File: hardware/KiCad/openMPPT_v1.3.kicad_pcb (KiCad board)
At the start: 2 copper layers, 70 x 80 mm, 135 parts, among them Q1 BSC030N08NS5, Q2 BSC030N08NS5, Q3 BSC030N08NS5, Q4 BSC030N08NS5, U1 STM32F072RBT6, U2 CC6937S8-3FB020, U3 CC6937S8-3FB020, U4 SCT2A25STER, U5 SY8120B1ABC

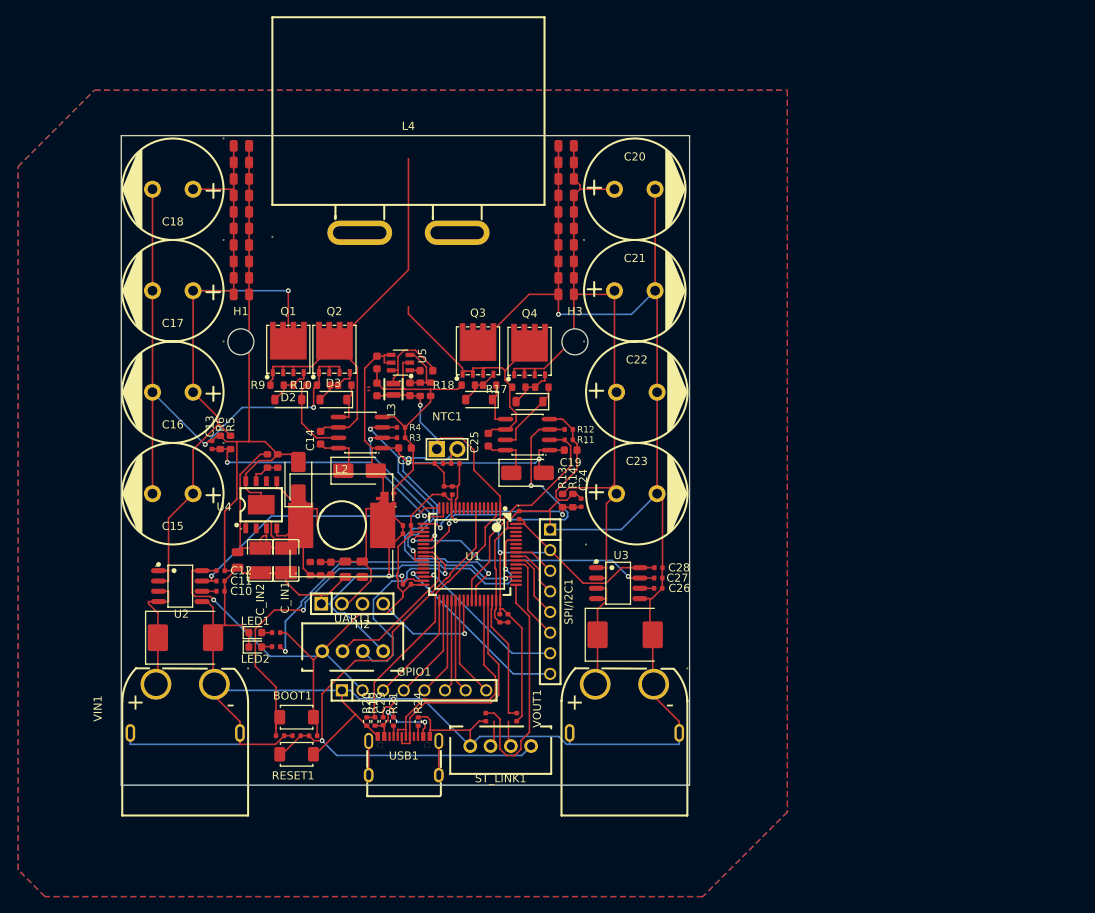
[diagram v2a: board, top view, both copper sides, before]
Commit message: hardware: import prior PCB layout work into current project
The current openMPPT_v1.3.kicad_pcb had footprints placed but zero
routing - the project's own PCB layout hadn't been started yet under
this repo structure. Real placement work already existed on the
now-stale feature/pcb-v1.3 branch (commit fe1c635 "started layout"),
done before the hardware/ reorg to the current file naming and library
layout. That branch never got merged and diverged too far from main to
merge normally, but the PCB layout itself is real prior work, not
throwaway - importing it here as the starting point instead of
re-placing 135 footprints from scratch.

Same KiCad file format version (20260206, pcbnew 10.0) on both sides,
so no format migration needed. Footprint/net sync against the current
schematic (which has moved on since this layout was done - D9 removed,
inductor/TVS parts changed) is the user's job in KiCad (Update PCB from
Schematic), not attempted here.

Co-Authored-By: Claude Sonnet 5 <noreply@anthropic.com>
Claude-Session: https://claude.ai/code/session_018pci5pMUxpfFa5RN5eKA6b
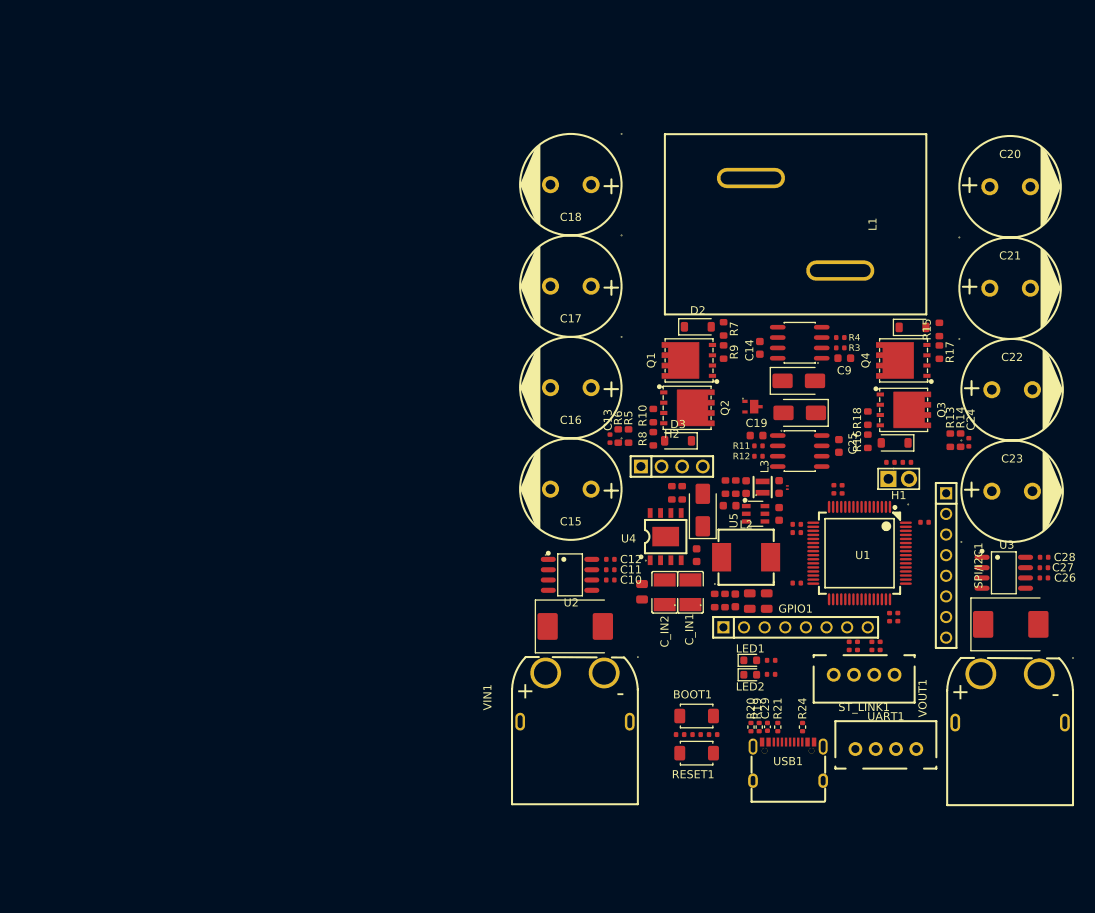
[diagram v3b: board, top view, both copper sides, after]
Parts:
- removed C1, C2, C3, C37, C38, C39, C4, C40, C41, C42, C43, C44, C45, C46, C47, C48, C5, C6, C7, C8: 100nF, PCM_JLCPCB:C_0805
- removed H3: MountingHole, MountingHole:MountingHole_3.2mm_M3_DIN965
- removed L4: HCZH-3218-150-M, easyeda2kicad:IND-TH_L33.5-W23.0-P12.00_HCZH-3218
- removed NTC1: TEMP, easyeda2kicad:HDR-TH_2P-P2.54-V-M
- removed R36, R37, R38, R39: 2.2Ω, PCM_JLCPCB:R_0603
- added L1: 47uH, easyeda2kicad:IND-TH_L32.2-W22.2_CPEX3222L, F.Cu at (133.9, 61.7)
- added R15: 5.1Ω, PCM_JLCPCB:R_0603, F.Cu at (151.6, 74.7)
- added R16: 5.1Ω, PCM_JLCPCB:R_0603, F.Cu at (142.8, 88.5)
- added R27: 47Ω, PCM_JLCPCB:R_0402, F.Cu at (143.3, 113.7)
- added R28: 47Ω, PCM_JLCPCB:R_0402, F.Cu at (141.5, 113.7)
- added R7: 5.1Ω, PCM_JLCPCB:R_0603, F.Cu at (125.0, 74.6)
- added R8: 5.1Ω, PCM_JLCPCB:R_0603, F.Cu at (116.3, 88.1)
- C14, C25: value 1uF -> 470nF
- D1, D4: value SS210 -> US1M
- D2, D3, D5, D6: value SS210 -> 1N4148W
- H1: value MountingHole -> TEMP; footprint MountingHole:MountingHole_3.2mm_M3_DIN965 -> easyeda2kicad:HDR-TH_2P-P2.54-V-M
- L2: footprint easyeda2kicad:IND-SMD_L12.5-W12.5-1 -> easyeda2kicad:IND-SMD_L7.7-W6.6_APS07A30M220
- LED1: value KT-0603R -> 19-213/Y2C-CQ2R2L/3T(CY)
- moved H1 82.8 mm to (146.6, 93.1)
- moved UART1 66.8 mm to (145.0, 126.3)
- moved LED1 61.1 mm to (128.3, 115.4)
- moved LED2 61.1 mm to (128.3, 117.2)
- moved R1 61.1 mm to (130.8, 115.4)
- moved R2 61.1 mm to (130.8, 117.2)
- moved R29 57.6 mm to (147.6, 91.0), turned to 0 degrees
- moved UA1 55.2 mm to (134.4, 76.3)
- moved C14 55.2 mm to (129.5, 76.9)
- moved C9 55.2 mm to (139.9, 78.2)
- moved D1 55.2 mm to (134.2, 81.0)
- moved R3 55.2 mm to (139.4, 76.9)
- moved R4 55.2 mm to (139.4, 75.7)
- moved R9 55.1 mm to (125.0, 77.5), turned to -90 degrees
- moved C31 53.6 mm to (145.5, 91.0), turned to 180 degrees
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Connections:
- net IN_CAP renamed Net-(C15-+)
- net OUT_CAP renamed Net-(C20-+)
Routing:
- net GND: track 582.1 -> 0.00 mm, vias 6 -> 0
- net 3V3: track 176.5 -> 0.00 mm, vias 5 -> 0
- net Net-(C20-+): track 90.9 -> 0.00 mm
- net Net-(C15-+): track 90.7 -> 0.00 mm, vias 1 -> 0
- net +10V: track 72.8 -> 0.00 mm, vias 2 -> 0
- net NRST: track 72.2 -> 0.00 mm, vias 1 -> 0
- net BOOT0: track 58.4 -> 0.00 mm, vias 2 -> 0
- net VS_A: track 54.8 -> 0.00 mm
- net TIM1_CH1N: track 37.6 -> 0.00 mm, vias 2 -> 0
- net LED: track 37.2 -> 0.00 mm, vias 2 -> 0
- net TIM1_CH2: track 37.2 -> 0.00 mm, vias 2 -> 0
- net VSENSEIN: track 34.5 -> 0.00 mm, vias 2 -> 0
- net ISENSEIN: track 34.0 -> 0.00 mm, vias 2 -> 0
- net VS_B: track 33.5 -> 0.00 mm
- net ISENSEOUT: track 33.2 -> 0.00 mm, vias 2 -> 0
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- removed copper zone on B.Cu, net GND
- removed copper zone on F.Cu, net GND
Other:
- board outline removed

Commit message: hardware: fix L4 footprint's broken 3D model path, sync PCB from schematic
The L4 footprint (IND-TH_L33.5-W23.0-P12.00_HCZH-3218) had a malformed
3D model path with a doubled directory segment:
${KIPRJMOD}/hardware/KiCad/libraries/... instead of
${KIPRJMOD}/libraries/... (KIPRJMOD already resolves to hardware/KiCad/,
the .kicad_pro's own directory) - so it silently failed to resolve,
looking like a missing/misaligned 3D model in the viewer rather than an
outright broken path. Re-saving the footprint in the Footprint Editor
fixed the path and, as a side effect, upgraded the whole file from the
legacy (module ...) format to the current (footprint "...") format -
KiCad does this automatically for any old-format footprint touched in a
new KiCad version.

Also includes the accumulated "Update PCB from Schematic" sync against
the current parts list (D9 removed, inductor swapped, etc. - the schema
has moved on since the imported layout was done on the old feature/pcb-v1.3
branch, per PR #8's description of remaining work).

Co-Authored-By: Claude Sonnet 5 <noreply@anthropic.com>
Claude-Session: https://claude.ai/code/session_018pci5pMUxpfFa5RN5eKA6b
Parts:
- removed D9: 3.3V, PCM_JLCPCB:D_DFN0603-2L
- removed L1: 47uH, easyeda2kicad:IND-TH_L32.2-W22.2_CPEX3222L
- removed R16: 5.1Ω, PCM_JLCPCB:R_0603
- removed R27, R28: 47Ω, PCM_JLCPCB:R_0402
- added C1: 100nF, PCM_JLCPCB:C_0805, F.Cu at (39.3, 84.5)
- added C2: 100nF, PCM_JLCPCB:C_0805, F.Cu at (39.3, 87.6)
- added C3: 100nF, PCM_JLCPCB:C_0805, F.Cu at (39.3, 90.6)
- added C37: 100nF, PCM_JLCPCB:C_0805, F.Cu at (43.8, 93.7)
- added C38: 100nF, PCM_JLCPCB:C_0805, F.Cu at (43.8, 96.7)
- added C39: 100nF, PCM_JLCPCB:C_0805, F.Cu at (48.2, 84.5)
- added C4: 100nF, PCM_JLCPCB:C_0805, F.Cu at (39.3, 93.7)
- added C40: 100nF, PCM_JLCPCB:C_0805, F.Cu at (48.2, 87.6)
- added C41: 100nF, PCM_JLCPCB:C_0805, F.Cu at (48.2, 90.6)
- added C42: 100nF, PCM_JLCPCB:C_0805, F.Cu at (48.2, 93.7)
- added C43: 100nF, PCM_JLCPCB:C_0805, F.Cu at (48.2, 96.7)
- added C44: 100nF, PCM_JLCPCB:C_0805, F.Cu at (52.7, 84.5)
- added C45: 100nF, PCM_JLCPCB:C_0805, F.Cu at (52.7, 87.6)
- added C46: 100nF, PCM_JLCPCB:C_0805, F.Cu at (52.7, 90.6)
- added C47: 100nF, PCM_JLCPCB:C_0805, F.Cu at (52.7, 93.7)
- added C48: 100nF, PCM_JLCPCB:C_0805, F.Cu at (52.7, 96.7)
- added C5: 100nF, PCM_JLCPCB:C_0805, F.Cu at (39.3, 96.7)
- added C6: 100nF, PCM_JLCPCB:C_0805, F.Cu at (43.8, 84.5)
- added C7: 100nF, PCM_JLCPCB:C_0805, F.Cu at (43.8, 87.6)
- added C8: 100nF, PCM_JLCPCB:C_0805, F.Cu at (43.8, 90.6)
- added H3: MountingHole, MountingHole:MountingHole_3.2mm_M3_DIN965, F.Cu at (91.0, 97.9)
- added L4: HCZH-3218-150-M, easyeda2kicad:IND-TH_L33.5-W23.0-P12.00_HCZH-3218, F.Cu at (133.6, 68.0)
- added NTC1: TEMP, easyeda2kicad:HDR-TH_2P-P2.54-V-M, F.Cu at (77.0, 55.7)
- added R36: 2.2Ω, PCM_JLCPCB:R_0603, F.Cu at (56.7, 84.1)
- added R37: 2.2Ω, PCM_JLCPCB:R_0603, F.Cu at (56.7, 86.4)
- added R38: 2.2Ω, PCM_JLCPCB:R_0603, F.Cu at (56.7, 88.6)
- added R39: 2.2Ω, PCM_JLCPCB:R_0603, F.Cu at (56.7, 90.9)
- C14, C25: value 470nF -> 1uF; footprint PCM_JLCPCB:C_0603 -> PCM_JLCPCB:C_0402
- D1, D4: value US1M -> SS210
- D2, D3, D5, D6: value 1N4148W -> SS210; footprint PCM_JLCPCB:D_SOD-123 -> PCM_JLCPCB:D_SMA
- H1: value TEMP -> MountingHole; footprint easyeda2kicad:HDR-TH_2P-P2.54-V-M -> MountingHole:MountingHole_3.2mm_M3_DIN965
- L2: footprint easyeda2kicad:IND-SMD_L7.7-W6.6_APS07A30M220 -> easyeda2kicad:IND-SMD_L12.5-W12.5-1
- LED1: value 19-213/Y2C-CQ2R2L/3T(CY) -> KT-0603R
- Q1, Q2, Q3, Q4: footprint easyeda2kicad:TDSON-8_L5.9-W5.2-P1.27-BL-1 -> easyeda2kicad:PG-TDSON-8_L5.0-W6.0-P1.27-BL-EP
- R15: value 5.1Ω -> 110kΩ
- R7, R8: value 5.1Ω -> 47Ω
- moved R30 1.56 mm to (123.9, 109.0)
- moved R35 1.56 mm to (118.6, 95.7)
- moved L2 1.56 mm to (126.5, 103.6)
- moved C32 1.56 mm to (125.2, 108.9)
- moved CC_Boot1 1.56 mm to (120.4, 103.4)
- moved C_IN1 1.56 mm to (119.6, 107.9)
- moved C_IN2 1.56 mm to (116.5, 108.0)
- moved C_IN_BYPASS1 1.56 mm to (113.7, 107.9)
- moved C_OUT2 1.56 mm to (126.9, 109.0)
- moved D7 1.56 mm to (121.2, 97.8)
- moved R31 1.56 mm to (122.6, 109.0)
- moved R34 1.56 mm to (117.3, 95.7)
- moved U4 1.56 mm to (116.6, 101.1)
- moved C_OUT1 1.56 mm to (129.0, 109.0)
- moved BOOT1 1.13 mm to (121.7, 121.2)
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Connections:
- net Net-(C15-+) renamed IN_CAP
- net Net-(C20-+) renamed OUT_CAP
- R15 pad 1: Net-(UB1-HO) -> unconnected-(R15-Pad1)
- R15 pad 2: HO_B -> unconnected-(R15-Pad2)
- R7 pad 1: Net-(UA1-HO) -> SWDIO
- R7 pad 2: HO_A -> Net-(R7-Pad2)
- R8 pad 1: Net-(UA1-LO) -> SWCLK
- R8 pad 2: LO_A -> Net-(R8-Pad2)
- ST_LINK1 pad 2: Net-(R28-Pad2) -> Net-(R8-Pad2)
- ST_LINK1 pad 3: Net-(R27-Pad2) -> Net-(R7-Pad2)
